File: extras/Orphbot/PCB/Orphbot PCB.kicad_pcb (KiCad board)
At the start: 2 copper layers, 100 x 100 mm, 21 parts, among them J1 Barrel_Jack, J2 Screw_Terminal_01x02, J3 Screw_Terminal_01x02, J4 Screw_Terminal_01x02, J5 Screw_Terminal_01x02, J7 Raspberry_Pi_4, J8 Conn_01x10_Pin, SW1 KFC7x7_Latching_DPDT, U1 MPU6050 Module, U10 SK6812 MINI E, U11 SK6812 MINI E, U2 DRV8833 MODULE, U3 DRV8833 MODULE, U4 0.96 OLED 128x64, U5 DROK BUCK MODULE, U6 SK6812 MINI E, U7 SK6812 MINI E, U8 SK6812 MINI E, U9 SK6812 MINI E

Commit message: Example PCB Polish Done
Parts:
- added G***: LOGO, LOGO, F.Cu at (48.8, 91.0)
- added G***: LOGO, LOGO, F.Cu at (104.2, 98.8)
- added G***: LOGO, LOGO, F.Cu at (75.8, 48.5)
- added G***: LOGO, LOGO, B.Cu at (55.9, 42.4)
- added G***: LOGO, LOGO, B.Cu at (-19.0, 95.9)
- added G***: LOGO, LOGO, B.Cu at (107.5, 83.9)
- added G***: LOGO, LOGO, B.Cu at (105.0, 101.8)
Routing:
- net GND: vias 77 -> 75
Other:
- board text added: "Designed By: Logan Peterson"
- board text added: "OrphBot"
- board text added: "Raspberry Pi Zero 2W Goes Here"

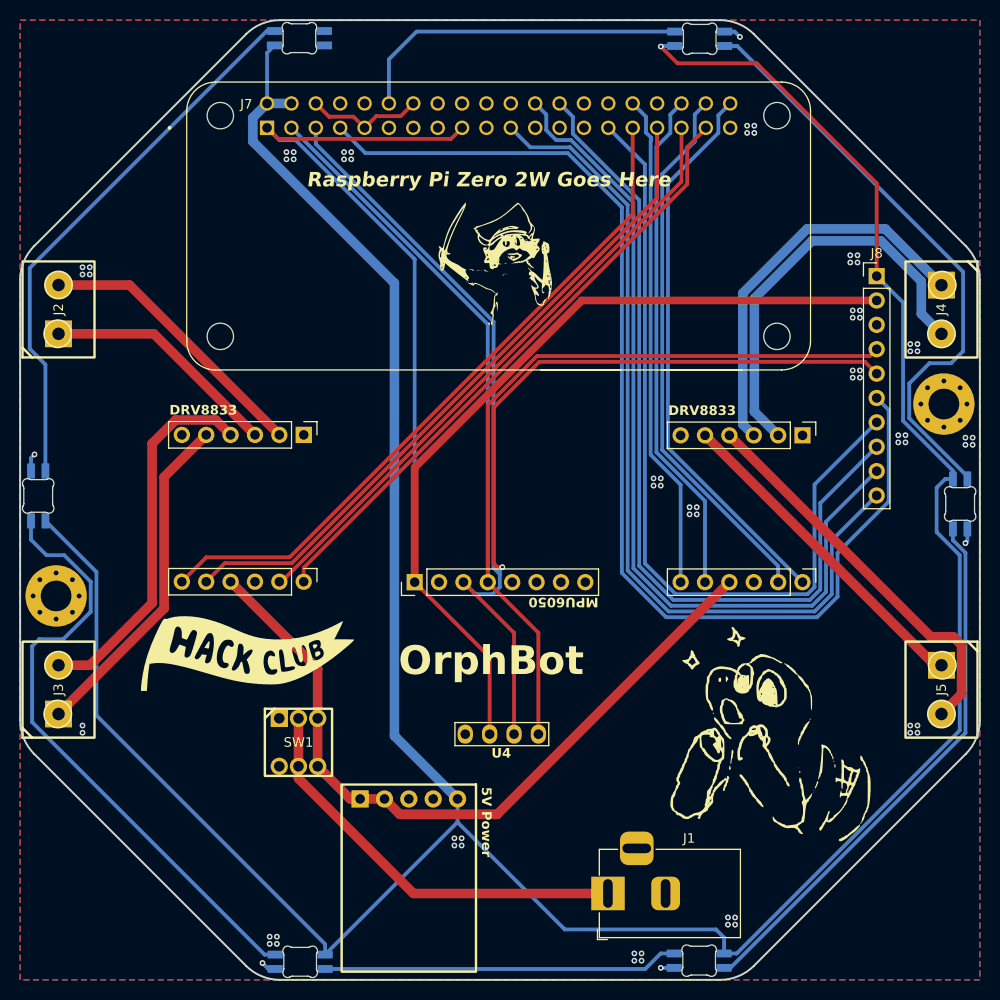
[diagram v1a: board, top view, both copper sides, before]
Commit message: Updated Example PCB
Added servo connector + flipped LEDs to be facing down.
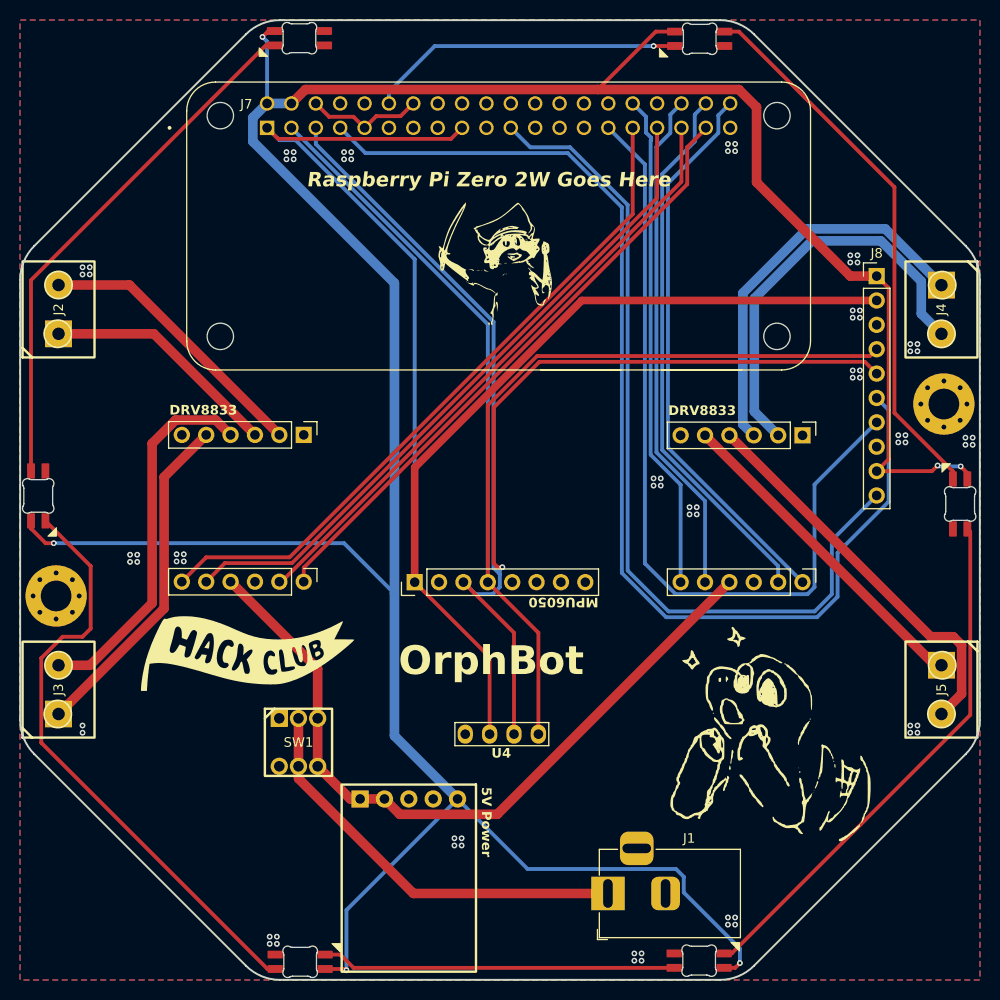
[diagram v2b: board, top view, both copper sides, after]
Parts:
- U10, U11, U6, U7, U8, U9: moved to B.Cu
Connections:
- J8 pad 8: /GPIO7 -> GND
- J8 pad 9: /GPIO8 -> +5V
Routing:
- net /GPIO8: track 90.6 -> 0.00 mm
- net /GPIO7: track 89.7 -> 0.00 mm
- net +5V: track 331.0 -> 316.4 mm, vias 1 -> 6
- net GND: track 20.5 -> 12.3 mm, vias 75 -> 78
- net Net-(U6-DOUT): track 62.3 -> 57.3 mm
- net /LED_DATA: track 35.6 -> 33.0 mm, vias 0 -> 1
- net Net-(U10-DOUT): track 57.6 -> 55.4 mm
- net Net-(U7-DOUT): track 57.1 -> 55.5 mm
- net Net-(U10-DIN): track 64.0 -> 62.6 mm

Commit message: Add PCB guide and update example PCB
Large update to the Orphbot PCB and docs.
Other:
- board text added: "3V3"
- board text added: "5V"
- board text added: "GND"
- board text added: "IO4"
- board text added: "IO5"
- board text added: "IO9"
- board text added: "M1"
- board text added: "M2"
- board text added: "M3"
- board text added: "M4"
- board text added: "SCL"
- board text added: "SDA"
